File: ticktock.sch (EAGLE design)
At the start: 35 parts, among them IC1 ATMEGA644A, IC2 AD8611R, J1 AVR_SPI_PRG_6NS, Q1 MOSFET-NCHANNEL2N7002PW, U1 MAX232SOIC16, U2 OSCILLATORSMD, U3 FT232RLSSOP

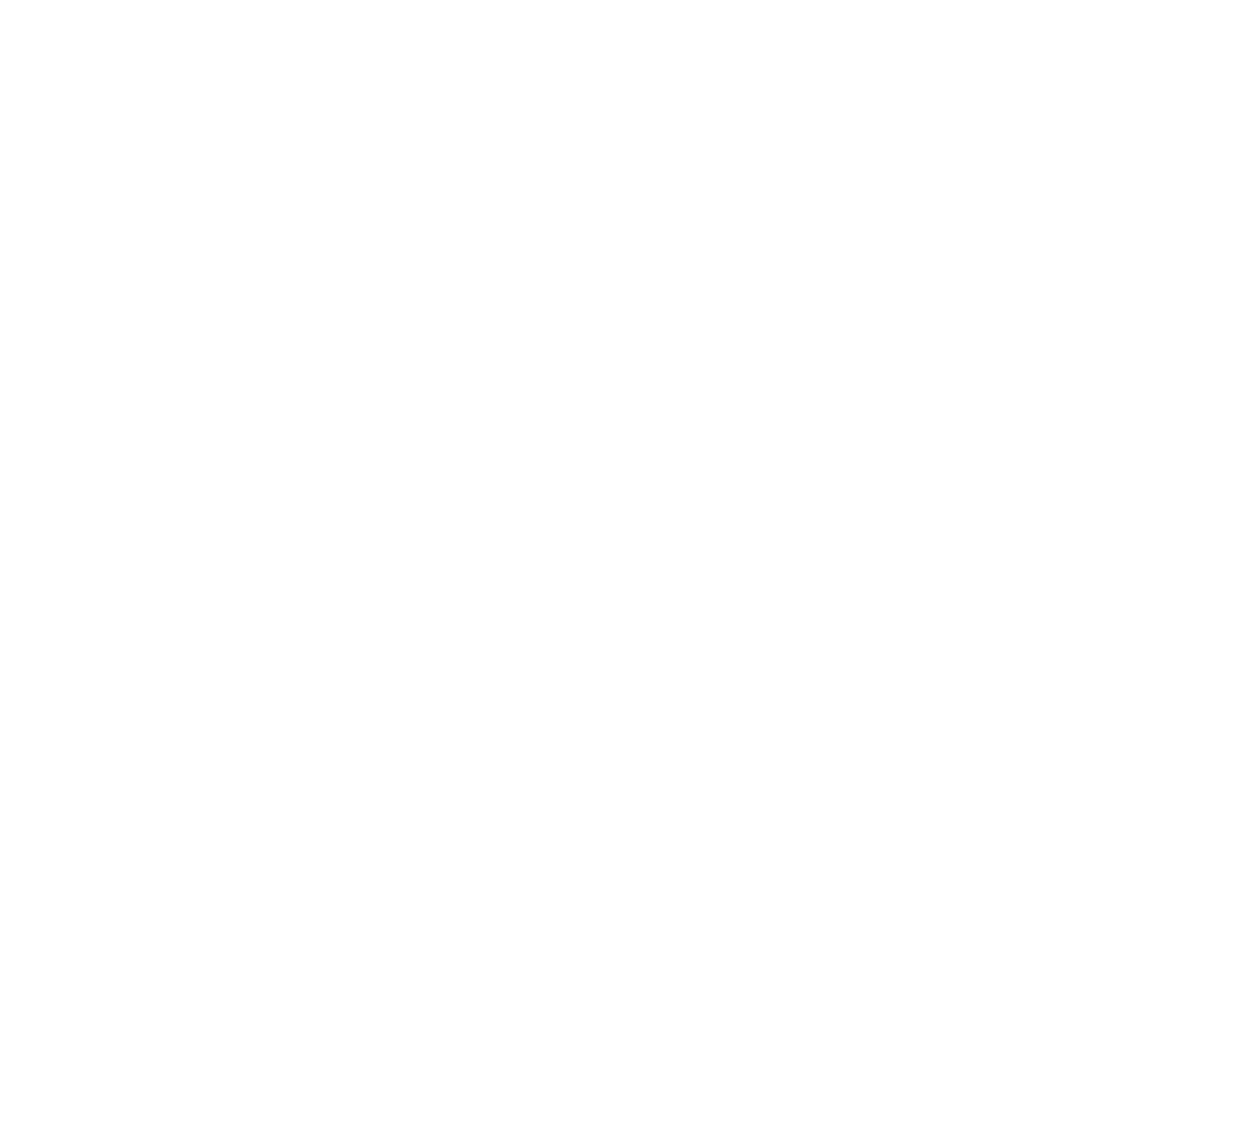
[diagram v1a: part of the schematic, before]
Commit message: Add thermistor 100/200uA current source
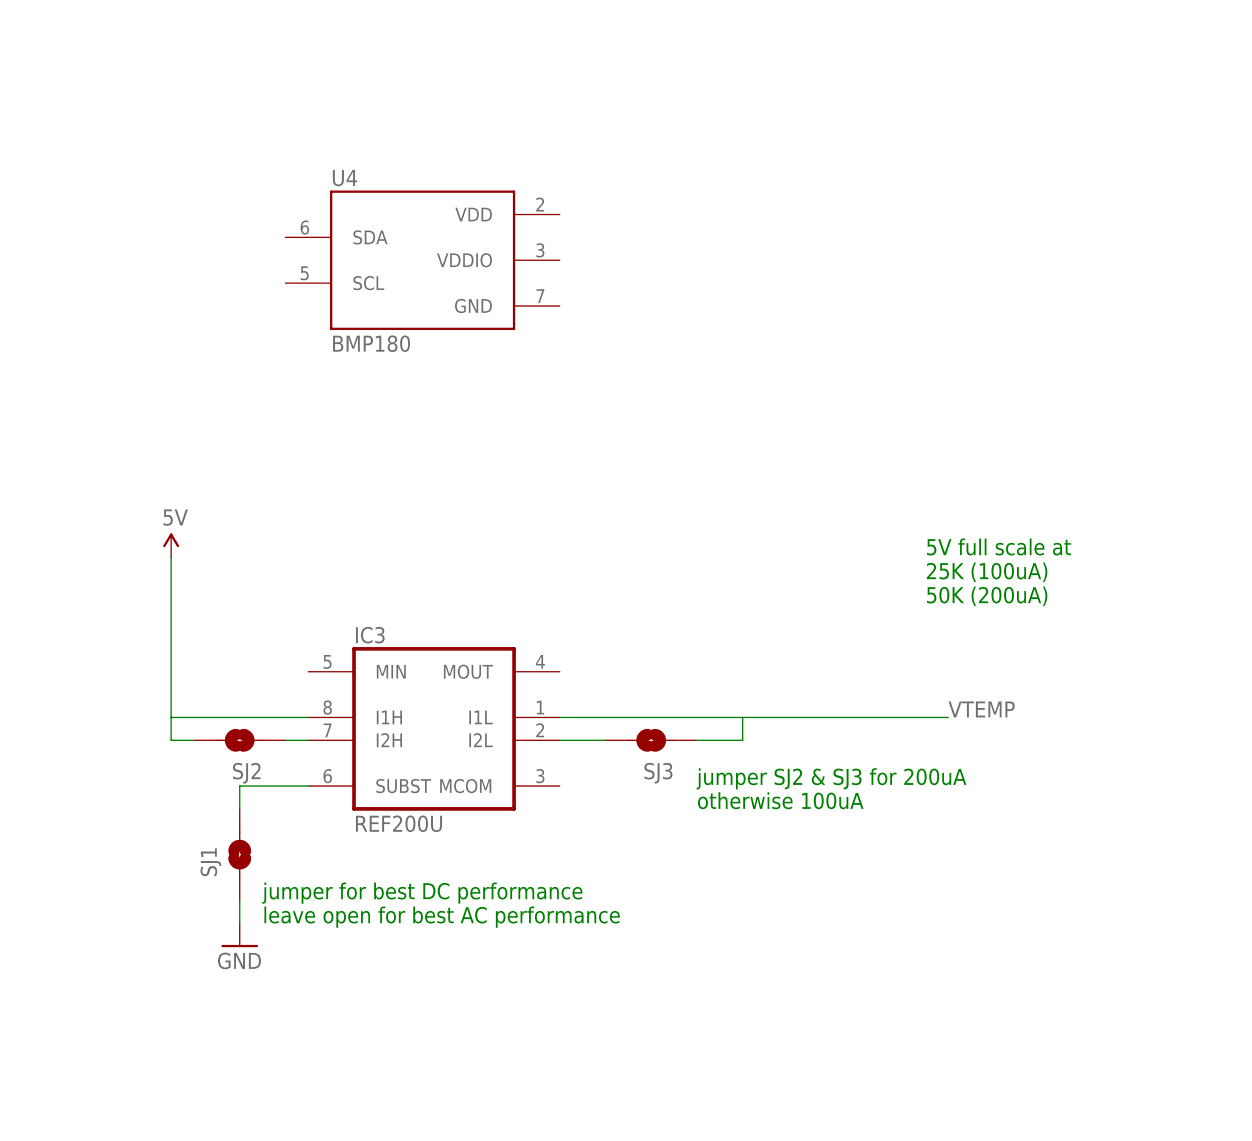
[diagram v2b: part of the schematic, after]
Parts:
- added IC3: REF200U, burr-brown:REF200U
- added SJ1, SJ2, SJ3: SOLDERJUMPERNO, SparkFun:SOLDERJUMPERNO
- added U4: BMP180, SparkFun-Sensors:BMP180
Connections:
- new net N$14: IC3.SUBST, SJ1.2
- new net N$17: IC3.I2H, SJ2.1
- new net N$19: IC3.I2L, SJ3.2
- net 5V: now also IC3.I1H, SJ2.2
- net GND: now also SJ1.1
- net VTEMP: now also IC3.I1L, SJ3.1
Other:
- note added: "5V full scale at 25K (100uA) 50K (200uA)"
- note added: "jumper SJ2 & SJ3 for 200uA otherwise 100uA"
- note added: "jumper for best DC performance leave open for best AC performance"
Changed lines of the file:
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@@
 <part name="U$1" library="tickTockLibrary" deviceset="OPA381" device=""/>
 <part name="GND22" library="SparkFun-Aesthetics" deviceset="GND" device=""/>
+<part name="U4" library="SparkFun-Sensors" deviceset="BMP180" device=""/>
+<part name="IC3" library="burr-brown" deviceset="REF200" device="U"/>
+<part name="SJ1" library="SparkFun" deviceset="SOLDERJUMPER" device="NO"/>
+<part name="GND23" library="SparkFun-Aesthetics" deviceset="GND" device=""/>
+<part name="SJ2" library="SparkFun" deviceset="SOLDERJUMPER" device="NO"/>
+<part name="SJ3" library="SparkFun" deviceset="SOLDERJUMPER" device="NO"/>
+<part name="SUPPLY19" library="SparkFun-Aesthetics" deviceset="5V" device=""/>
 </parts>
 <sheets>
@@
 CASE = cathode = IN-</text>
 <text x="182.88" y="398.78" size="1.778" layer="91">PD_CATHODE = GND</text>
+<text x="347.98" y="99.06" size="1.778" layer="91">jumper for best DC performance
+leave open for best AC performance</text>
+<text x="396.24" y="111.76" size="1.778" layer="91">jumper SJ2 &amp; SJ3 for 200uA
+otherwise 100uA</text>
+<text x="421.64" y="134.62" size="1.778" layer="91">5V full scale at
+25K (100uA)
+50K (200uA)</text>
 </plain>
 <instances>
@@
 <instance part="U$1" gate="G$1" x="109.22" y="281.94"/>
 <instance part="GND22" gate="1" x="210.82" y="396.24"/>
+<instance part="U4" gate="G$1" x="365.76" y="172.72"/>
+<instance part="IC3" gate="G$1" x="368.3" y="119.38"/>
+<instance part="SJ1" gate="1" x="345.44" y="106.68" rot="R90"/>
+<instance part="GND23" gate="1" x="345.44" y="96.52"/>
+<instance part="SJ2" gate="1" x="345.44" y="119.38" rot="R180"/>
+<instance part="SJ3" gate="1" x="391.16" y="119.38" rot="R180"/>
+<instance part="SUPPLY19" gate="G$1" x="337.82" y="139.7"/>
 </instances>
 <busses>
@@
 <wire x1="243.84" y1="403.86" x2="210.82" y2="403.86" width="0.1524" layer="91"/>
 </segment>
+<segment>
+<pinref part="GND23" gate="1" pin="GND"/>
+<pinref part="SJ1" gate="1" pin="1"/>
+<wire x1="345.44" y1="99.06" x2="345.44" y2="101.6" width="0.1524" layer="91"/>
+</segment>
 </net>
 <net name="IR_PWM" class="0">
@@
 <pinref part="AMPC1" gate="G$1" pin="1"/>
 <wire x1="96.52" y1="248.92" x2="99.06" y2="248.92" width="0.1524" layer="91"/>
+</segment>
+<segment>
+<pinref part="IC3" gate="G$1" pin="I1H"/>
+<wire x1="353.06" y1="121.92" x2="337.82" y2="121.92" width="0.1524" layer="91"/>
+<wire x1="337.82" y1="121.92" x2="337.82" y2="139.7" width="0.1524" layer="91"/>
+<pinref part="SJ2" gate="1" pin="2"/>
+<wire x1="340.36" y1="119.38" x2="337.82" y2="119.38" width="0.1524" layer="91"/>
+<wire x1="337.82" y1="119.38" x2="337.82" y2="121.92" width="0.1524" layer="91"/>
+<pinref part="SUPPLY19" gate="G$1" pin="5V"/>
 </segment>
 </net>
@@
 <label x="190.5" y="381" size="1.778" layer="95"/>
 </segment>
-</net>
+<segment>
+<pinref part="IC3" gate="G$1" pin="I1L"/>
+<wire x1="381" y1="121.92" x2="401.32" y2="121.92" width="0.1524" layer="91"/>
+<pinref part="SJ3" gate="1" pin="1"/>
+<wire x1="401.32" y1="121.92" x2="424.18" y2="121.92" width="0.1524" layer="91"/>
+<wire x1="396.24" y1="119.38" x2="401.32" y2="119.38" width="0.1524" layer="91"/>
+<wire x1="401.32" y1="119.38" x2="401.32" y2="121.92" width="0.1524" layer="91"/>
+<label x="424.18" y="121.92" size="1.778" layer="95"/>
+</segment>
+</net>
+<net name="N$14" class="0">
+<segment>
+<pinref part="SJ1" gate="1" pin="2"/>
+<wire x1="345.44" y1="111.76" x2="345.44" y2="114.3" width="0.1524" layer="91"/>
+<pinref part="IC3" gate="G$1" pin="SUBST"/>
+<wire x1="345.44" y1="114.3" x2="353.06" y2="114.3" width="0.1524" layer="91"/>
+</segment>
+</net>
+<net name="N$17" class="0">
+<segment>
+<pinref part="IC3" gate="G$1" pin="I2H"/>
+<pinref part="SJ2" gate="1" pin="1"/>
+<wire x1="353.06" y1="119.38" x2="350.52" y2="119.38" width="0.1524" layer="91"/>
+</segment>
+</net>
+<net name="N$19" class="0">
+<segment>
+<pinref part="IC3" gate="G$1" pin="I2L"/>
+<pinref part="SJ3" gate="1" pin="2"/>
+<wire x1="381" y1="119.38" x2="386.08" y2="119.38" width="0.1524" layer="91"/>
+</segment>
+</net>

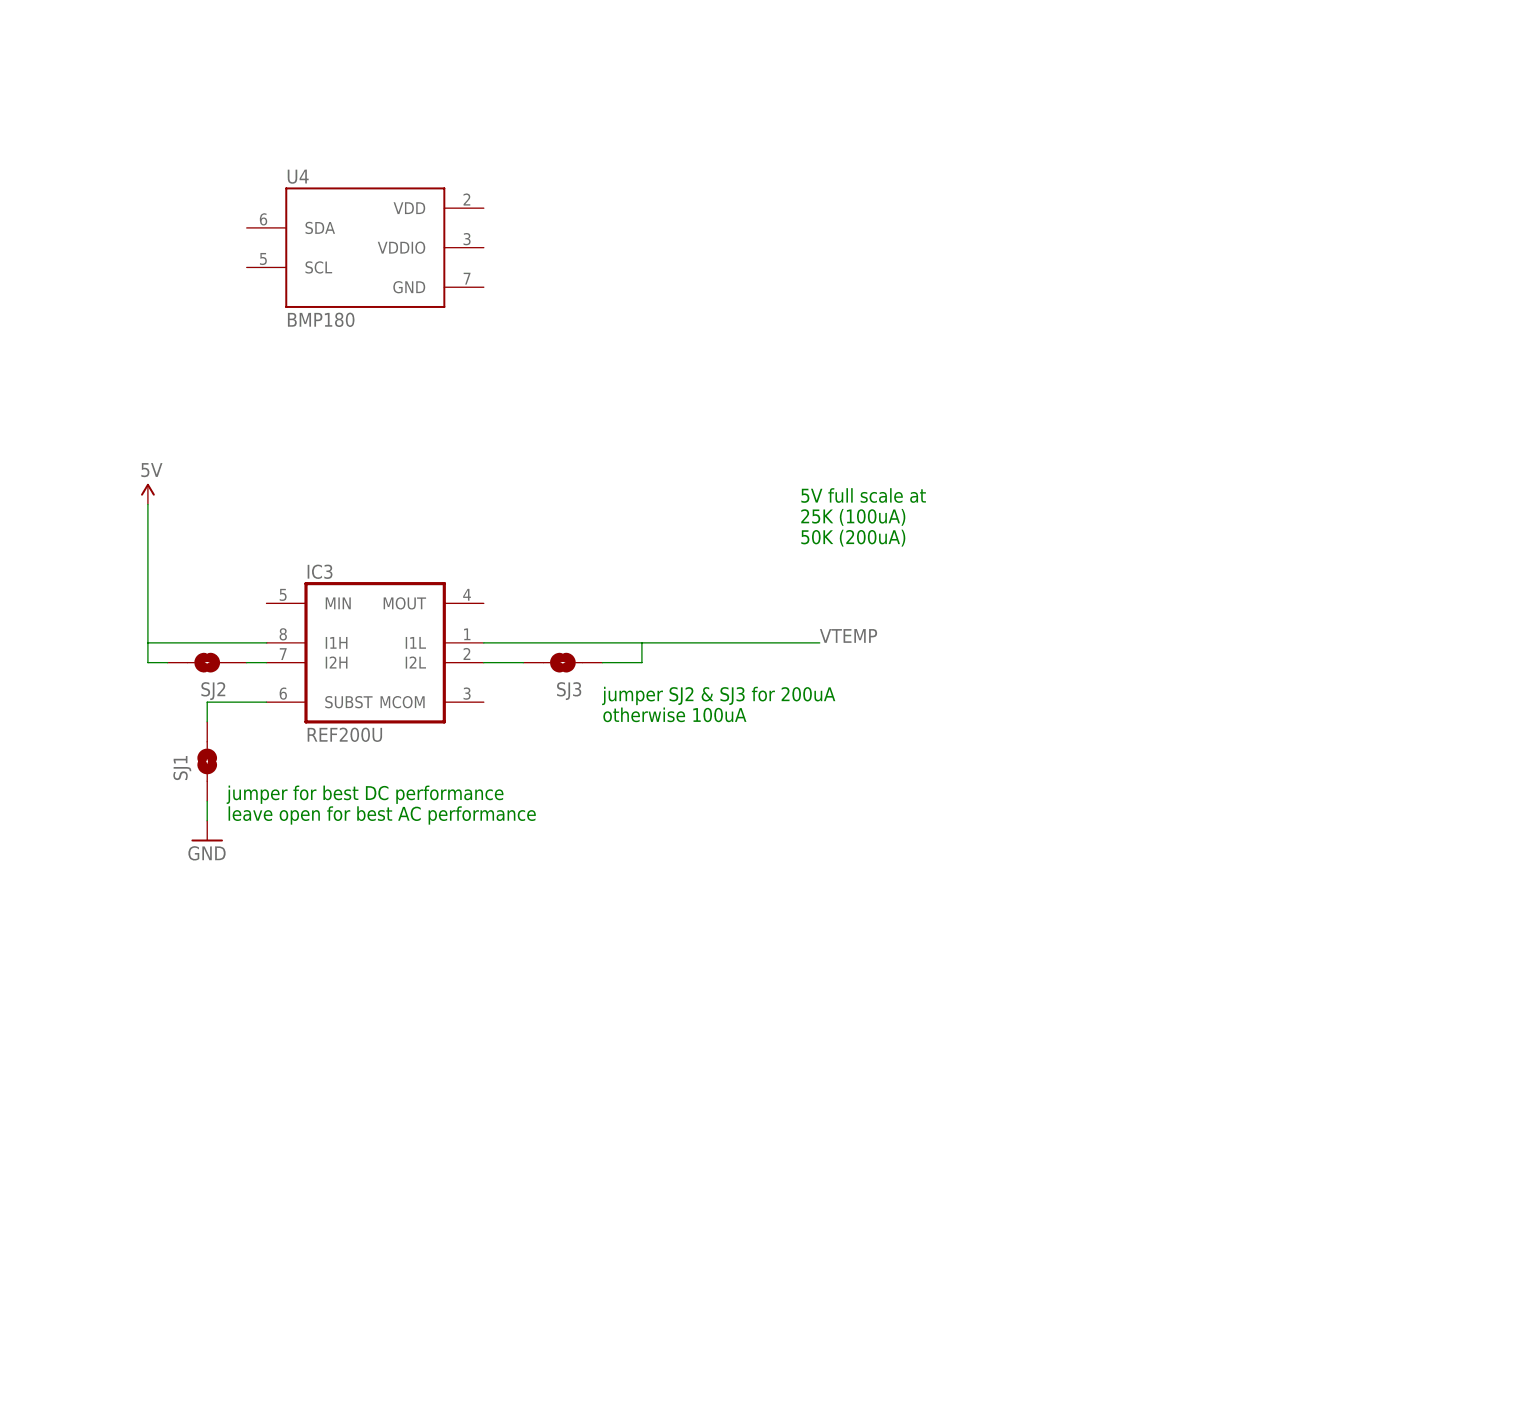
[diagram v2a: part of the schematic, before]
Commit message: Add BMP180 and level shifters
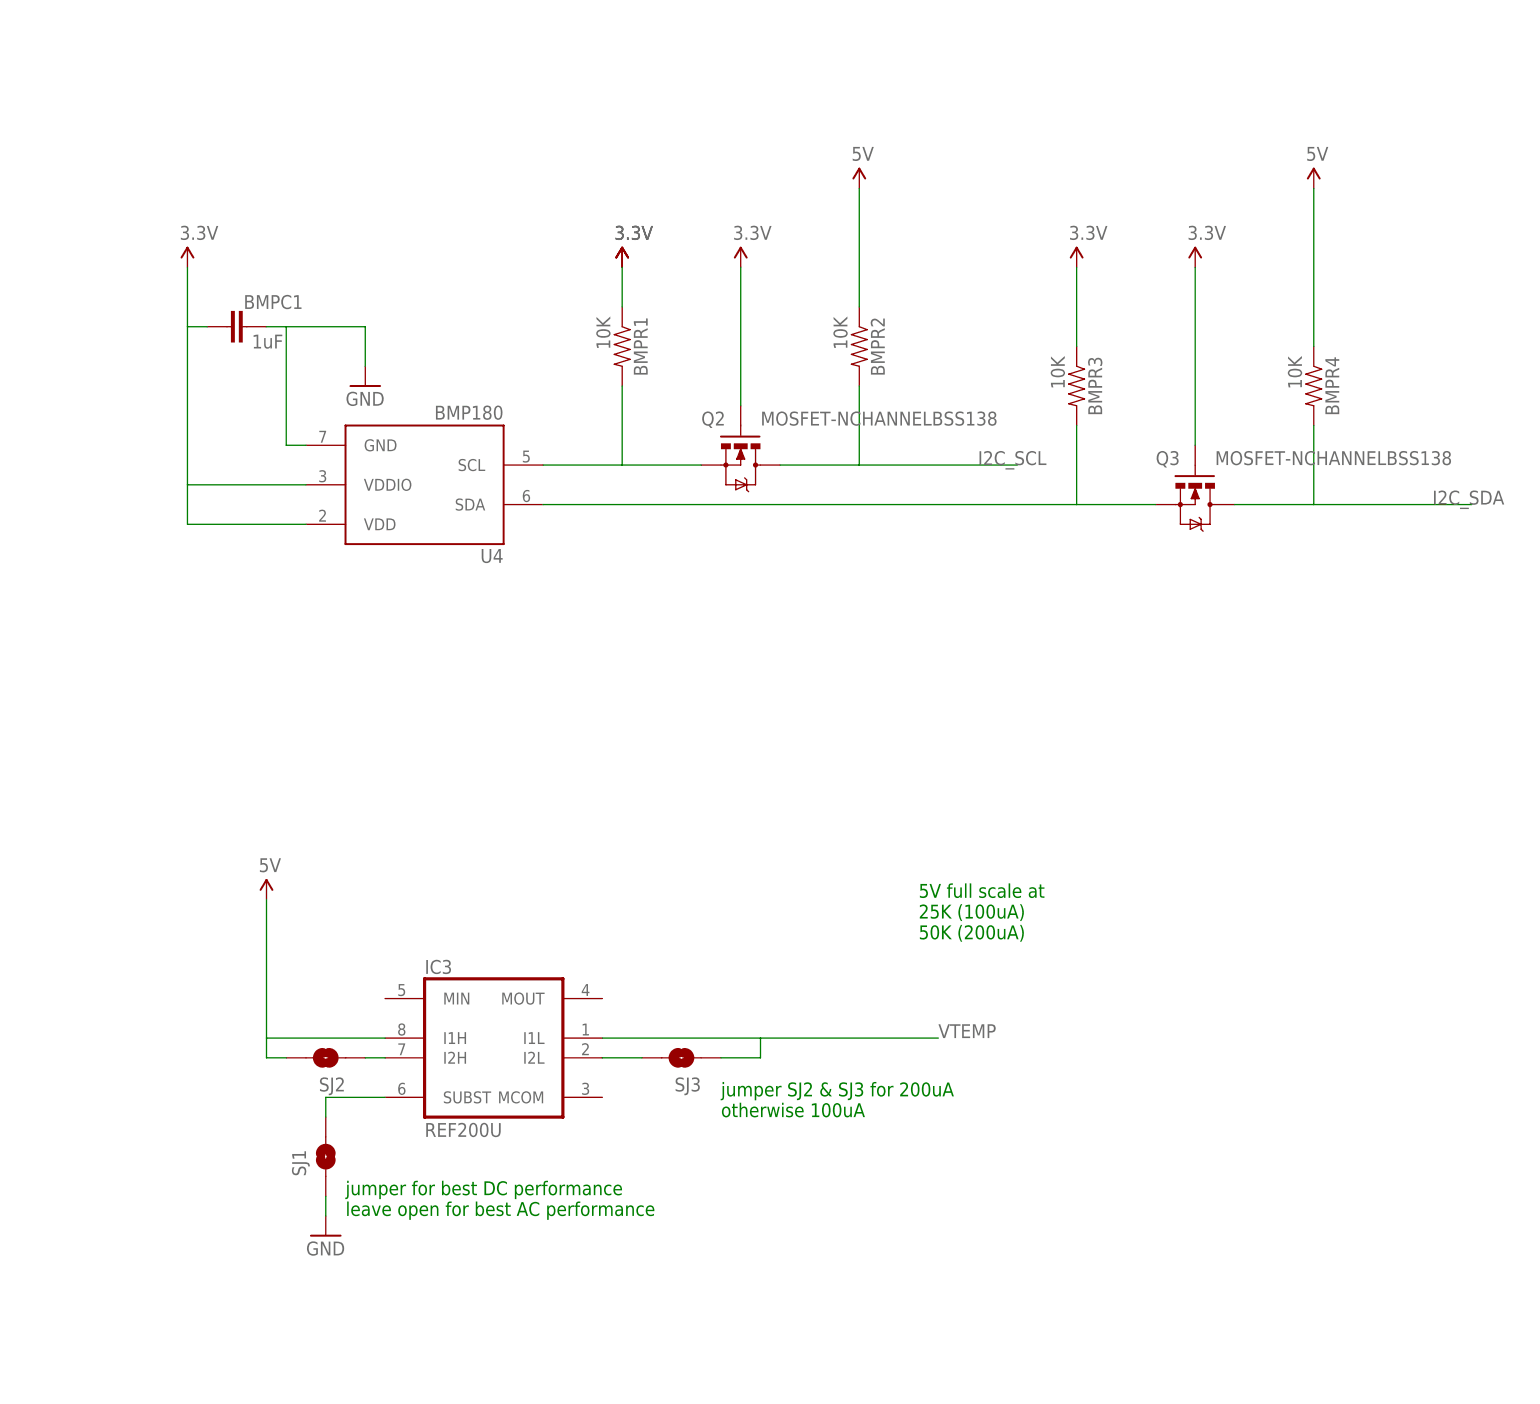
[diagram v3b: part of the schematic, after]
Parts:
- added BMPC1: 1uF, SparkFun-Capacitors:CAP0805
- added BMPR1, BMPR2, BMPR3, BMPR4: 10K, SparkFun-Resistors:RESISTOR0805-RES
- added Q2, Q3: MOSFET-NCHANNELBSS138, SparkFun-DiscreteSemi:MOSFET-NCHANNELBSS138
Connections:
- new net I2C_SCL: BMPR2.2, Q2.D
- new net I2C_SDA: BMPR4.2, Q3.D
- new net N$15: BMPR1.2, Q2.S, U4.SCL
- new net N$18: BMPR3.2, Q3.S, U4.SDA
- net 3.3V: now also BMPC1.1, BMPR1.1, BMPR3.1, Q2.G, Q3.G, U4.VDD, U4.VDDIO
- net 5V: now also BMPR2.1, BMPR4.1
- net GND: now also BMPC1.2, U4.GND
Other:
- moved on the sheet: IC3, SJ1, SJ2, SJ3, U4
